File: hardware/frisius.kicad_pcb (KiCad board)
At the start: 4 copper layers, 40 x 60 mm, 135 parts, among them J1 Conn_02x25_Odd_Even_Shielded, J3 USB_C_Receptacle, J4 MEM2067, Q1 Q_NMOS_DGS, Q2 MBT2222ADW1T1, SW1 OVERRIDE, SW4 SW_Push, U1 ESP32-PICO-V3-02, U10 CP2102N-Axx-xQFN24, U11 PAC194x-1, U12 RT5789, U2 FXOS8700CQR1, U3 MS5637-02BA03, U4 L96-M33, U5 MAX77751, U6 LM75B, U7 MAX17048G, U8 NCV8187AMLExCG, U9 NCV8187AMLExCG

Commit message: Updates
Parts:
- removed AE1: 2.4G, RF_Antenna:Johanson_2450AT18x100
- removed C1, C10, C17, C19, C29, C3, C37, C38, C39, C5, C53, C6, C7, C8, C9: 0.1u, Capacitor_SMD:C_0402_1005Metric
- removed C18, C43, C54: 4.7u, Capacitor_SMD:C_0603_1608Metric
- removed C2, C26, C31, C32, C33, C34, C4, C44, C45, C46: 1u, Capacitor_SMD:C_0402_1005Metric
- removed C40, C41, C42, C48, C49: 10u, Capacitor_SMD:C_0603_1608Metric
- removed C47: 10p, Capacitor_SMD:C_0402_1005Metric
- removed D1, D11, D2, D6: LED_Small_Filled, LED_SMD:LED_0603_1608Metric
- removed D5: MBR0540, LED_SMD:LED_0603_1608Metric
- removed D7: SK6805, LED_SMD:LED_SK6805_PLCC4_2.4x2.7mm_P1.3mm
- removed the D8 at (136.4, 127.7)
- removed J1: Conn_02x25_Odd_Even_Shielded, Connector_Molex:Molex_SlimStack_55560-0501_2x25_P0.50mm_Vertical
- removed J3: USB_C_Receptacle, bt_Connector_USB:AMPHENOL_124019032112A
- removed J4: MEM2067, bt_Connector_uSD:GCT_MEM2067-02-180-00-A_REVB
- removed L1, R16, R23, R26, R27, R59, R8, R9: 0, Resistor_SMD:R_0402_1005Metric
- removed L2: L_Small, Inductor_SMD:L_0402_1005Metric
- removed L4: 1u, Inductor_SMD:L_Wuerth_MAPI-2510
- removed N3: ShieldCan_ESP, RF_Shielding:Laird_Technologies_BMI-S-101_13.66x12.70mm
- removed N6: Display Board, Fiducial:Fiducial_0.5mm_Mask1.5mm
- removed Q1: Q_NMOS_DGS, Package_TO_SOT_SMD:SOT-323_SC-70
- removed Q2: MBT2222ADW1T1, Package_TO_SOT_SMD:SOT-363_SC-70-6
- removed R1, R12, R28, R29, R36, R38: 100k, Resistor_SMD:R_0402_1005Metric
- removed R10, R13, R22, R5: 1k, Resistor_SMD:R_0402_1005Metric
- removed R18: CORE_SENSE, bt_Resistor:R_0805_4WKelvin
- removed R30, R31, R44, R45, R46, R47, R48, R49: 10k, Resistor_SMD:R_0402_1005Metric
- removed R32, R33, R34, R35, R41, R42: 22, Resistor_SMD:R_0402_1005Metric
- removed R37: ?, Resistor_SMD:R_0402_1005Metric
- removed R6: DISP_SENSE, bt_Resistor:R_0805_4WKelvin
- removed SW1: OVERRIDE, Button_Switch_SMD:SW_DIP_SPSTx04_Slide_Omron_A6H-4101_W6.15mm_P1.27mm
- removed SW4: SW_Push, Button_Switch_SMD:SW_SPST_B3U-1000P
- removed U1: ESP32-PICO-V3-02, Package_DFN_QFN:QFN-48-1EP_7x7mm_P0.5mm_EP5.3x5.3mm
- removed U10: CP2102N-Axx-xQFN24, Package_DFN_QFN:QFN-24-1EP_4x4mm_P0.5mm_EP2.6x2.6mm
- removed U11: PAC194x-1, bt_Package_QFN:VQFN-16-1EP_3x3mm_P0.5mm_EP1.2x1.2mm
- removed U12: RT5789, Package_TO_SOT_SMD:TSOT-23-8
- removed U5: MAX77751, bt_Package_QFN:FC2QFN-24-3x3_P0.4mm
- removed U6: LM75B, bt_Package_SON:XSON-8U
- removed U8, U9: NCV8187AMLExCG, Package_DFN_QFN:DFN-8-1EP_3x3mm_P0.65mm_EP1.55x2.4mm
- added ?: , , F.Cu at (124.0, 122.2)
- added D8: LED_Small_Filled, LED_SMD:LED_0402_1005Metric, F.Cu at (113.4, 153.7)
- added D8: LED_Small_Filled, LED_SMD:LED_0402_1005Metric, F.Cu at (118.4, 153.7)
- added D8: LED_Small_Filled, LED_SMD:LED_0402_1005Metric, F.Cu at (88.2, 152.8)
- added D9: LED_Small_Filled, LED_SMD:LED_0402_1005Metric, F.Cu at (87.0, 152.8)
- added H1: BL, MountingHole:MountingHole_2.5mm_Pad_Via, F.Cu at (81.0, 122.2)
- added REF**: ESP32-S3-WROOM-1U, RF_Module:ESP32-S3-WROOM-1U, F.Cu at (117.9, 137.0)
- added REF**: QFN-24-1EP_4x4mm_P0.5mm_EP2.7x2.6mm_ThermalVias, Package_DFN_QFN:QFN-24-1EP_4x4mm_P0.5mm_EP2.7x2.6mm_ThermalVias, F.Cu at (70.3, 181.1)
- added REF**: SW_SPST_B3U-1000P-B, Button_Switch_SMD:SW_SPST_B3U-1000P-B, F.Cu at (113.4, 150.6)
- added REF**: SW_SPST_B3U-1000P-B, Button_Switch_SMD:SW_SPST_B3U-1000P-B, F.Cu at (118.4, 150.6)
- added REF**: AMPHENOL_124019032112A, bt_Connector_USB:AMPHENOL_124019032112A, F.Cu at (102.5, 152.8)
- added REF**: PinHeader_2x14_P2.54mm_Vertical, Connector_PinHeader_2.54mm:PinHeader_2x14_P2.54mm_Vertical, F.Cu at (86.0, 123.5)
- added REF**: U.FL_Molex_MCRF_73412-0110_Vertical, Connector_Coaxial:U.FL_Molex_MCRF_73412-0110_Vertical, F.Cu at (80.8, 143.8)
- added REF**: GCT_MEM2067-02-180-00-A_REVB, bt_Connector_uSD:GCT_MEM2067-02-180-00-A_REVB, B.Cu at (118.0, 137.0)
- D3: footprint LED_SMD:LED_0603_1608Metric -> LED_SMD:LED_0402_1005Metric
- R7: value AUX_SENSE -> 1k; footprint bt_Resistor:R_0805_4WKelvin -> Resistor_SMD:R_0402_1005Metric
- U4: moved to F.Cu
- moved C28 102.0 mm to (67.0, 188.3), turned to 0 degrees
- moved C30 100.8 mm to (70.3, 188.5), turned to 0 degrees
- moved BT1 98.8 mm to (66.3, 185.8), turned to 90 degrees
- moved U7 97.5 mm to (70.4, 185.9), turned to 90 degrees
- moved C23 96.3 mm to (55.8, 173.5), turned to -90 degrees
- moved C27 96.0 mm to (55.8, 175.9), turned to 90 degrees
- moved C25 94.7 mm to (57.1, 172.8), turned to -90 degrees
- moved R14 93.9 mm to (58.3, 168.9), turned to 90 degrees
- moved R15 92.5 mm to (59.3, 168.9), turned to 90 degrees
- moved C21 90.3 mm to (60.8, 169.4), turned to 0 degrees
- moved C24 88.8 mm to (60.9, 175.9), turned to -90 degrees
- moved R24 87.8 mm to (62.6, 168.9), turned to -90 degrees
- moved R25 86.4 mm to (63.6, 168.9), turned to -90 degrees
- moved C20 86.3 mm to (62.9, 175.9)
- moved R11 86.3 mm to (72.5, 176.7), turned to 0 degrees
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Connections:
- R17 pad 1: VDD_SYS_3V5 -> Net-(D8-Pad1)
- R7 pad 1: VDD_AUX_3V3 -> Net-(D9-Pad1)
- R7 pad 2: /Power/VDD_AUX_SNS- -> Net-(R7-Pad2)
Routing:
- net GND: track 16.5 -> 0.00 mm
- net VDD_SYS_3V5: track 16.2 -> 0.00 mm, vias 1 -> 0
- net Net-(C9-Pad1): track 5.17 -> 0.00 mm
- net VBUS: track 4.70 -> 0.00 mm
- net VDD_NVDC: track 4.29 -> 0.00 mm, vias 4 -> 0
- net /Processor/3V3_ESP_VDDA_FILT: track 3.75 -> 0.00 mm
- net Net-(C47-Pad2): track 3.38 -> 0.00 mm
- net Net-(L4-Pad1): track 2.79 -> 0.00 mm
- net /USB/DTR_BASE: track 2.41 -> 0.00 mm, vias 1 -> 0
- net /USB/CP2102N_DTR: track 2.25 -> 0.00 mm
- net /USB/~{RTS}_BASE: track 2.25 -> 0.00 mm
- net VBUS_OVP: track 1.73 -> 0.00 mm
- net /USB/CP2102N_D+: track 1.72 -> 0.00 mm
- net /USB/CP2102N_D-: track 1.71 -> 0.00 mm
- net /USB/CP2102N_RTS: track 1.39 -> 0.00 mm
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- removed copper zone on B.Cu, net GND
- removed copper zone on F.Cu, net GND
- removed copper zone on In1.Cu, net GND
- removed copper zone on F.Cu, net Net-(C22-Pad2)
- removed copper zone on In2.Cu, net VDD_AUX_3V3
- removed copper zone on In2.Cu, net VDD_CORE_3V3
- removed copper zone on F.Cu, net VDD_NVDC
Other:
- board size 40 x 60 mm -> 50 x 36.6 mm
- board text removed: "AUX"
- board text removed: "BATT"
- board text removed: "NVDC"
- board text removed: "SYS"
- board text removed: "VBUS"

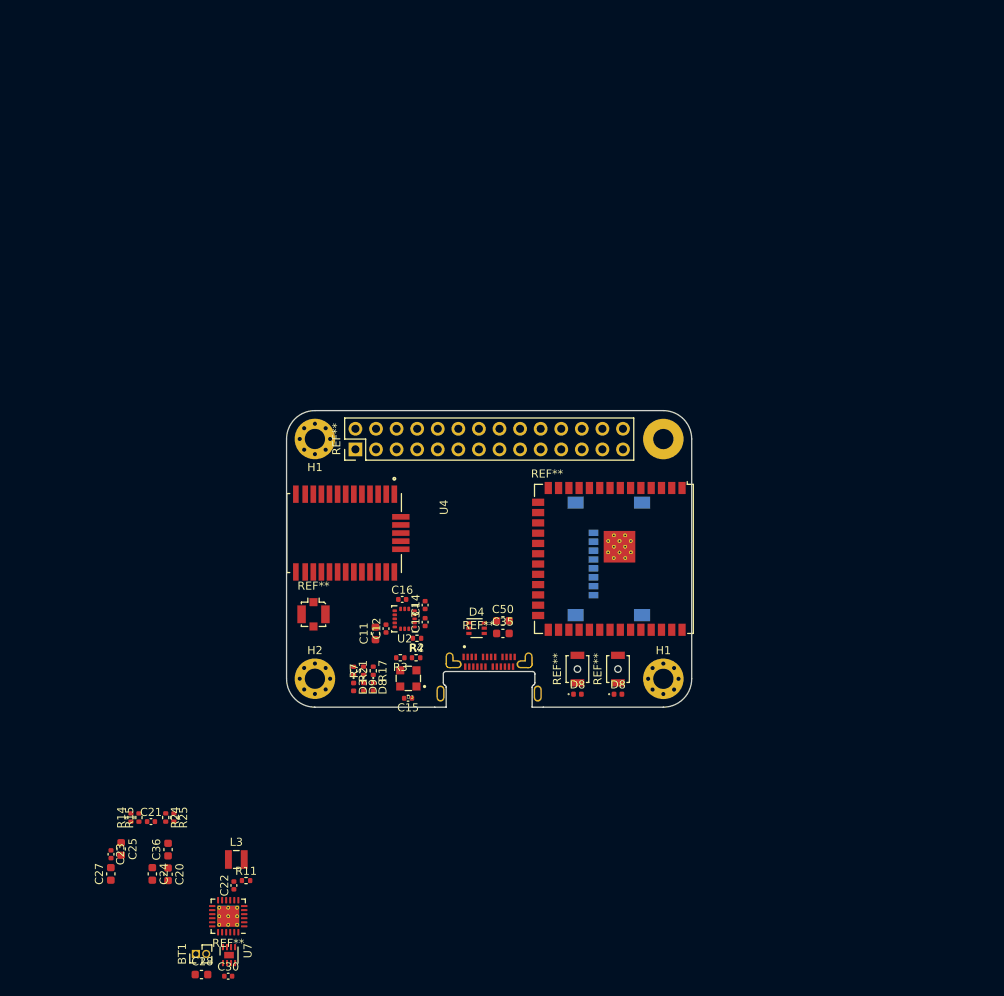
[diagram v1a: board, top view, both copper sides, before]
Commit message: layout 0 unconnected
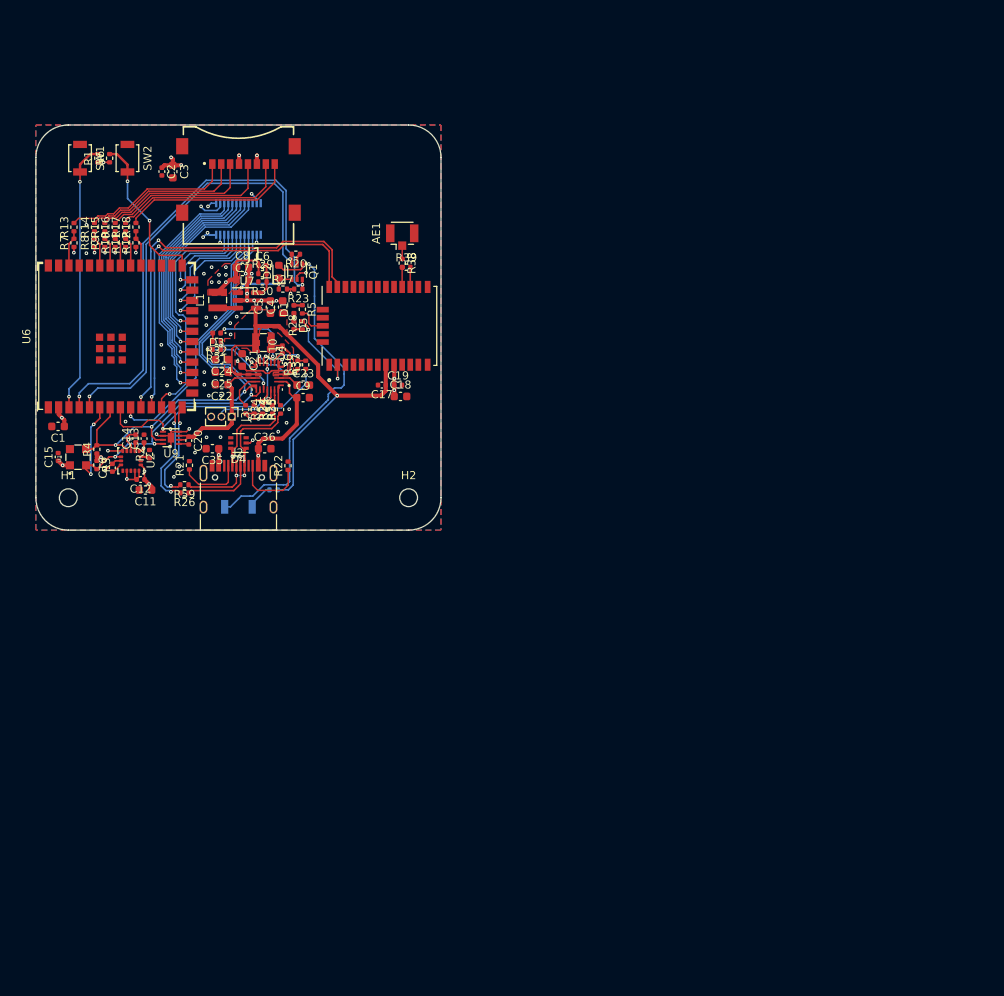
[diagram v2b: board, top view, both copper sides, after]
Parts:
- removed ?: , 
- removed BT1: JST-PH-2, Connector_PinHeader_1.27mm:PinHeader_1x02_P1.27mm_Vertical
- removed C27, C28: 10u, Capacitor_SMD:C_0603_1608Metric
- removed C30: 0.1u, Capacitor_SMD:C_0402_1005Metric
- removed C50: 4.7u, Capacitor_SMD:C_0603_1608Metric
- removed D8 (x3), D9: LED_Small_Filled, LED_SMD:LED_0402_1005Metric
- removed the H1 at (124.0, 151.8)
- removed the H1 at (81.0, 122.2)
- removed L3: 0.47u, Inductor_SMD:L_Wuerth_MAPI-2510
- removed REF**: ESP32-S3-WROOM-1U, RF_Module:ESP32-S3-WROOM-1U
- removed REF**: QFN-24-1EP_4x4mm_P0.5mm_EP2.7x2.6mm_ThermalVias, Package_DFN_QFN:QFN-24-1EP_4x4mm_P0.5mm_EP2.7x2.6mm_ThermalVias
- removed REF** (x2): SW_SPST_B3U-1000P-B, Button_Switch_SMD:SW_SPST_B3U-1000P-B
- removed REF**: AMPHENOL_124019032112A, bt_Connector_USB:AMPHENOL_124019032112A
- removed REF**: PinHeader_2x14_P2.54mm_Vertical, Connector_PinHeader_2.54mm:PinHeader_2x14_P2.54mm_Vertical
- removed REF**: U.FL_Molex_MCRF_73412-0110_Vertical, Connector_Coaxial:U.FL_Molex_MCRF_73412-0110_Vertical
- removed REF**: GCT_MEM2067-02-180-00-A_REVB, bt_Connector_uSD:GCT_MEM2067-02-180-00-A_REVB
- added AE1: Antenna_Shield, Connector_Coaxial:U.FL_Hirose_U.FL-R-SMT-1_Vertical, F.Cu at (91.8, 97.3)
- added C1: 4.7u, Capacitor_SMD:C_0603_1608Metric, F.Cu at (49.3, 120.7)
- added C10: 0.1u, Capacitor_SMD:C_0402_1005Metric, F.Cu at (77.0, 111.2)
- added C17: 0.1u, Capacitor_SMD:C_0402_1005Metric, F.Cu at (89.3, 115.5)
- added C18: 4.7u, Capacitor_SMD:C_0603_1608Metric, F.Cu at (91.6, 117.0)
- added C19: 0.1u, Capacitor_SMD:C_0402_1005Metric, F.Cu at (91.3, 115.5)
- added C2: 0.1u, Capacitor_SMD:C_0402_1005Metric, F.Cu at (62.1, 89.2)
- added C3: 4.7u, Capacitor_SMD:C_0603_1608Metric, F.Cu at (63.5, 89.2)
- added C4: 4.7u, Capacitor_SMD:C_0603_1608Metric, F.Cu at (77.0, 105.9)
- added C5: 4.7u, Capacitor_SMD:C_0603_1608Metric, F.Cu at (75.5, 105.9)
- added C6: 10p, Capacitor_SMD:C_0402_1005Metric, F.Cu at (74.5, 100.8)
- added C7: 10u, Capacitor_SMD:C_0603_1608Metric, F.Cu at (72.0, 102.5)
- added C8: 10u, Capacitor_SMD:C_0603_1608Metric, F.Cu at (72.0, 101.0)
- added C9: 4.7u, Capacitor_SMD:C_0603_1608Metric, F.Cu at (79.5, 117.1)
- added D1: LED_Small_Filled, LED_SMD:LED_0402_1005Metric, F.Cu at (78.4, 106.2)
- added D2: MBR0540, LED_SMD:LED_0603_1608Metric, F.Cu at (76.5, 101.5)
- added D5: LED_Small_Filled, LED_SMD:LED_0402_1005Metric, F.Cu at (78.4, 108.2)
- added H1: BL, MountingHole:MountingHole_2.2mm_M2_ISO7380, F.Cu at (50.6, 129.4)
- added J1: MEM2067, bt_Connector_uSD:GCT_MEM2067-02-180-00-A_REVB, F.Cu at (71.6, 90.9)
- added J2: USB_C_Receptacle_USB2.0, Connector_USB:USB_C_Receptacle_HRO_TYPE-C-31-M-12, F.Cu at (71.6, 129.6)
- added J3: BATTERY, Connector_PinHeader_1.27mm:PinHeader_1x03_P1.27mm_Vertical, F.Cu at (70.7, 119.5)
- added J4: Display, Connector_Molex:Molex_SlimStack_55560-0241_2x12_P0.50mm_Vertical, B.Cu at (71.6, 95.0)
- added L1: 1u, Inductor_SMD:L_Wuerth_MAPI-2510, F.Cu at (69.0, 105.0)
- added L2: 0.47u, Inductor_SMD:L_Wuerth_MAPI-2510, F.Cu at (74.7, 110.3)
- added N6: Display Board, Symbol:WEEE-Logo_4.2x6mm_SilkScreen, B.Cu at (238.1, 68.7)
- added Q1: Q_Dual_NMOS_G1S2G2D2S1D1, Package_TO_SOT_SMD:SOT-363_SC-70-6, F.Cu at (78.8, 101.5)
- added R1: R_Small, Resistor_SMD:R_0402_1005Metric, F.Cu at (54.2, 87.5)
- added R10: 10k, Resistor_SMD:R_0402_1005Metric, F.Cu at (56.4, 98.0)
- added R12: 10k, Resistor_SMD:R_0402_1005Metric, F.Cu at (58.9, 98.0)
- added R13: 22, Resistor_SMD:R_0402_1005Metric, F.Cu at (51.3, 96.1)
- added R16: 22, Resistor_SMD:R_0402_1005Metric, F.Cu at (56.4, 96.1)
- added R18: 22, Resistor_SMD:R_0402_1005Metric, F.Cu at (58.9, 96.0)
- added R19: 100k, Resistor_SMD:R_0402_1005Metric, B.Cu at (75.9, 128.5)
- added R20: 100k, Resistor_SMD:R_0402_1005Metric, F.Cu at (78.7, 99.4)
- added R22: 0, Resistor_SMD:R_0402_1005Metric, F.Cu at (77.7, 125.5)
- added R23: 100k, Resistor_SMD:R_0402_1005Metric, F.Cu at (79.0, 103.7)
- added R26: 0, Resistor_SMD:R_0402_1005Metric, F.Cu at (64.9, 128.8)
- added R27: 100k, Resistor_SMD:R_0402_1005Metric, F.Cu at (77.0, 103.7)
- added R28: 1k, Resistor_SMD:R_0402_1005Metric, F.Cu at (79.5, 108.2)
- added R29: ?, Resistor_SMD:R_0402_1005Metric, F.Cu at (74.5, 101.8)
- added R30: 100k, Resistor_SMD:R_0402_1005Metric, F.Cu at (74.5, 102.8)
- added R31: 1k, Resistor_SMD:R_0402_1005Metric, F.Cu at (68.9, 111.2)
- added R32: 1k, Resistor_SMD:R_0402_1005Metric, F.Cu at (68.9, 110.2)
- added R33: 0, Resistor_SMD:R_0402_1005Metric, F.Cu at (73.5, 118.5)
- added R34: 0, Resistor_SMD:R_0402_1005Metric, F.Cu at (72.5, 118.5)
- added R35: 14k, Resistor_SMD:R_0402_1005Metric, F.Cu at (74.5, 118.6)
- added R36: 14k, Resistor_SMD:R_0402_1005Metric, F.Cu at (78.9, 113.0)
- added R37: 14k, Resistor_SMD:R_0402_1005Metric, F.Cu at (79.9, 113.0)
- added R38: 0, Resistor_SMD:R_0402_1005Metric, F.Cu at (91.8, 100.5)
- added R39: 0, Resistor_SMD:R_0402_1005Metric, F.Cu at (92.3, 101.0)
- added R5: 1k, Resistor_SMD:R_0402_1005Metric, F.Cu at (79.5, 106.2)
- added R59: 0, Resistor_SMD:R_0402_1005Metric, F.Cu at (64.9, 127.8)
- added R6: R_Small, Resistor_SMD:R_0402_1005Metric, F.Cu at (55.7, 87.5)
- added R8: 10k, Resistor_SMD:R_0402_1005Metric, F.Cu at (53.8, 98.0)
- added R9: 10k, Resistor_SMD:R_0402_1005Metric, F.Cu at (55.1, 98.0)
- added SW1: RESET, Button_Switch_SMD:SW_SPST_B3U-1000P, F.Cu at (52.0, 87.5)
- added SW2: BOOT, Button_Switch_SMD:SW_SPST_B3U-1000P, F.Cu at (57.9, 87.5)
- added SW3: POWER, Button_Switch_SMD:SW_SPST_B3U-1000P, B.Cu at (71.6, 130.6)
- added U6: ESP32-S3-WROOM-1, bt_Espressif:ESP32-S3-WROOM-1U, F.Cu at (56.4, 109.5)
- added U8: MP2723, bt_Package_QFN:MP_QFN-26-3.5x3.5_P0.45mm, F.Cu at (75.1, 114.5)
- added U9: MAX17048G, Package_DFN_QFN:TDFN-8-1EP_2x2mm_P0.5mm_EP0.8x1.2mm, F.Cu at (63.2, 122.0)
- C20: value 4.7u -> 0.1u; footprint Capacitor_SMD:C_0603_1608Metric -> Capacitor_SMD:C_0402_1005Metric
- C21, C23: value 1u -> 10u; footprint Capacitor_SMD:C_0402_1005Metric -> Capacitor_SMD:C_0603_1608Metric
- C22: value 0.1u -> 10u; footprint Capacitor_SMD:C_0402_1005Metric -> Capacitor_SMD:C_0603_1608Metric
- H2: footprint MountingHole:MountingHole_2.5mm_Pad_Via -> MountingHole:MountingHole_2.2mm_M2_ISO7380
- R11: value 100k -> 10k
- R14, R15: value 14k -> 22
- R17: value 1k -> 22
- R21: value 1k -> 0
- R7: value 1k -> 10k
- U7: value MAX17048G -> TLV62569DBV; footprint Package_DFN_QFN:TDFN-8-1EP_2x2mm_P0.5mm_EP0.8x1.2mm -> Package_TO_SOT_SMD:SOT-23-5
- moved U7 80.8 mm to (72.6, 105.1), turned to 0 degrees
- moved R11 80.1 mm to (57.6, 98.0), turned to 90 degrees
- moved R14 73.0 mm to (53.8, 96.1)
- moved R15 73.0 mm to (55.1, 96.1)
- moved C24 64.1 mm to (69.5, 112.4), turned to 180 degrees
- moved R7 63.8 mm to (51.3, 98.0)
- moved R17 62.7 mm to (57.6, 96.1), turned to 90 degrees
- moved C23 62.6 mm to (79.6, 115.5), turned to 0 degrees
- moved C22 61.8 mm to (69.5, 115.5), turned to 180 degrees
- moved C25 60.1 mm to (69.5, 114.0), turned to 180 degrees
- moved C21 58.1 mm to (72.0, 112.5), turned to -90 degrees
- moved C20 53.6 mm to (65.4, 122.4)
- moved C15 52.5 mm to (49.3, 124.4), turned to 90 degrees
- moved R24 52.0 mm to (75.8, 118.6), turned to 90 degrees
- moved R25 52.0 mm to (76.8, 118.6), turned to 90 degrees
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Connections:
- net /USB/PORT_D+ renamed /Power/PORT_D+
- net /USB/PORT_D- renamed /Power/PORT_D-
- C11 pad 1: VDD_AUX_3V3 -> +3V3
- C12 pad 1: VDD_AUX_3V3 -> +3V3
- C13 pad 1: Net-(C13-Pad1) -> +3V3
- C15 pad 1: VDD_AUX_3V3 -> +3V3
- C20 pad 1: VBUS -> +BATT
- C21 pad 1: Net-(C21-Pad1) -> /Power/VREF
- C22 pad 1: Net-(C22-Pad1) -> +BATT
- C22 pad 2: Net-(C22-Pad2) -> GND
- C24 pad 1: VBUS_OVP -> VDD_NVDC
- D3 pad 2: VDD_NVDC -> Net-(D3-Pad2)
- D4 pad 3: /BMS/USB_CC.1 -> unconnected-(D4-Pad3)
- D4 pad 4: /BMS/USB_CC.2 -> unconnected-(D4-Pad4)
- R11 pad 1: Net-(Q1-Pad2) -> +3V3
- R11 pad 2: VDD_NVDC -> /Processor/SDMMC.D0
- R14 pad 1: Net-(R14-Pad1) -> /Processor/SDMMC.D3
- R14 pad 2: GND -> Net-(J1-Pad2)
- R15 pad 1: Net-(R15-Pad1) -> /Processor/SDMMC.CMD
- R15 pad 2: GND -> Net-(J1-Pad3)
- R17 pad 1: Net-(D8-Pad1) -> /Processor/SDMMC.D0
- R21 pad 2: Net-(D3-Pad1) -> GND
- R24 pad 2: /BMS/USB_CHG.D- -> /Power/USB_CHG.D-
- R25 pad 2: /BMS/USB_CHG.D+ -> /Power/USB_CHG.D+
- R3 pad 1: VDD_AUX_3V3 -> +3V3
- R3 pad 2: /BMS/SENSOR_I2C.SDA -> /Display/SYS_I2C.SDA
- R4 pad 1: VDD_AUX_3V3 -> +3V3
- R4 pad 2: /BMS/SENSOR_I2C.SCL -> /Display/SYS_I2C.SCL
- R7 pad 1: Net-(D9-Pad1) -> +3V3
- R7 pad 2: Net-(R7-Pad2) -> /Processor/SDMMC.D2
- U2 pad 1: Net-(C13-Pad1) -> +3V3
- U2 pad 14: VDD_AUX_3V3 -> +3V3
- U2 pad 4: /BMS/SENSOR_I2C.SCL -> /Display/SYS_I2C.SCL
- U2 pad 6: /BMS/SENSOR_I2C.SDA -> /Display/SYS_I2C.SDA
- U3 pad 1: VDD_AUX_3V3 -> +3V3
- U3 pad 2: /BMS/SENSOR_I2C.SDA -> /Display/SYS_I2C.SDA
- U3 pad 3: /BMS/SENSOR_I2C.SCL -> /Display/SYS_I2C.SCL
- U4 pad 16: /GPS/GPS_RF -> /GPS/MOD_RF
- U4 pad 2: Net-(TP11-Pad1) -> /GPS/L96_FIX
- U4 pad 3: Net-(R23-Pad1) -> unconnected-(U4-Pad3)
- U4 pad 6: Net-(R27-Pad1) -> unconnected-(U4-Pad6)
- U4 pad 9: VDD_AUX_3V3 -> +3V3
- U7 pad 1: GND -> Net-(D2-Pad1)
- U7 pad 2: +BATT -> GND
- U7 pad 3: +BATT -> Net-(L1-Pad1)
- U7 pad 4: GND -> VDD_NVDC
- U7 pad 5: unconnected-(U7-Pad5) -> Net-(C6-Pad2)
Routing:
- net /Display/SYS_I2C.SDA: track 0.00 -> 65.2 mm, vias 0 -> 5
- net /Power/POWER_BUTTON: track 0.00 -> 61.9 mm, vias 0 -> 2
- net /Display/SYS_I2C.SCL: track 0.00 -> 59.4 mm, vias 0 -> 3
- net /Power/SHUTDOWN: track 0.00 -> 56.1 mm, vias 0 -> 2
- net GND: track 0.00 -> 53.6 mm, vias 0 -> 53
- net VDD_NVDC: track 0.00 -> 52.7 mm, vias 0 -> 1
- net /GPS/GPS_UART.RX: track 0.00 -> 48.9 mm, vias 0 -> 2
- net /GPS/GPS_UART.TX: track 0.00 -> 46.6 mm, vias 0 -> 2
- net Net-(D2-Pad2): track 0.00 -> 45.7 mm, vias 0 -> 1
- net +3V3: track 0.00 -> 44.5 mm, vias 0 -> 29
- net /Processor/RST_BTN: track 0.00 -> 33.3 mm, vias 0 -> 2
- net /Display/TOUCH_INT: track 0.00 -> 31.6 mm, vias 0 -> 1
- net /Display/DISPLAY_BL: track 0.00 -> 29.5 mm, vias 0 -> 1
- net /Display/LCD_SPI_CTRL: track 0.00 -> 29.1 mm, vias 0 -> 1
- net /Display/RGB.R0: track 0.00 -> 28.3 mm, vias 0 -> 1
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- added copper zone on F.Cu, net +3V3
- added copper zone on In2.Cu, net +3V3
- added copper zone on B.Cu, net GND
- added copper zone on F.Cu, net GND
- added copper zone on In1.Cu, net GND
- added copper zone on F.Cu, net Net-(C10-Pad2)
- added copper zone on F.Cu, net VDD_NVDC
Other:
- board size 50 x 36.6 mm -> 50 x 50 mm
